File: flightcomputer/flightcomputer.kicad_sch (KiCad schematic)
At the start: 81 parts, among them J1 Conn_Coaxial, J10 Conn_01x03, J11 Conn_01x03, J12 ESQ-113-14-G-D, J13 Conn_01x07, J2 Conn_Coaxial, J3 Conn_Coaxial, J4 Conn_Coaxial, J5 S3B-PH-K-S-GW, J6 S3B-PH-K-S-GW, J7 S4B-PH-K-S_LF__SN_, J8 S3B-PH-K-S-GW, J9 Conn_01x06, U1 MAX-M10S, U2 LIS2MDLTR, U3 BMI088, U4 MS5607-02BA, U5 ESP32-S3-WROOM-1-N4, U7 Teensy4.1, U8 LSM6DSO32TR, U9 RFM96W-433S2

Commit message: resize
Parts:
- removed R16: 0, Resistor_SMD:R_0603_1608Metric_Pad0.98x0.95mm_HandSolder, symbol Device:R
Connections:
- net 5V: no longer J12.13, J12.15, J12.17
- net GND: now also J12.13, J12.15, J12.17; no longer J12.01, J12.03, J12.05
- net PYRO1: no longer J12.24
- net PYRO2: no longer J12.26
- net SENSE_miso: no longer J12.16
- net SENSE_mosi: no longer J12.14
- net SENSE_sck: no longer J12.18
- net aux7_rx: no longer J12.06
- net aux7_tx: no longer J12.08
- net can_rx: no longer J12.10
- net can_tx: no longer J12.12
- net servo1_pwm: no longer J12.22
- net servo2_pwm: no longer J12.20
- net teensy_3.3v: no longer R15.2
- net at J12.04: no longer R15.1
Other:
- moved on the sheet: J12, R15

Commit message: flight computer routing
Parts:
- removed J6, J8: S3B-PH-K-S-GW, HPRlibrary:S3BPHKSGW, symbol HPRlibrary:S3B-PH-K-S-GW
- removed TP15, TP16, TP17, TP18, TP5, TP6, TP7, TP8: TestPoint, Connector_PinHeader_2.54mm:PinHeader_1x01_P2.54mm_Vertical, symbol Connector:TestPoint
- added J14: S3B-PH-K-S-GW, HPRlibrary:S3BPHKSGW, symbol HPRlibrary:S3B-PH-K-S-GW
- added J6, J8: Conn_01x03, Connector_PinHeader_2.54mm:PinHeader_1x03_P2.54mm_Vertical, symbol Connector_Generic:Conn_01x03
- TP1: footprint Connector_PinSocket_2.54mm:PinSocket_1x01_P2.54mm_Vertical -> Connector_PinHeader_2.54mm:PinHeader_1x01_P2.54mm_Vertical
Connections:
- net aux2_rx is gone; now on net PYRO2CONN: U7.9 (7_RX2_OUT1A)
- net aux2_tx is gone; now on net PYRO1CONN: U7.10 (8_TX2_IN1)
- net aux7_rx is gone; now on net lsmimu_int: U7.20 (28_RX7)
- net aux7_tx is gone; now on net lsmimu_cs: U7.21 (29_TX7)
- net 5v_cursns: now also U7.33 (41_A17)
- net 5v_fault: now also U7.32 (40_A16)
- net 6v_cursns: now also U7.45 (23_A9_CRX1_MCLK1)
- net 6v_fault: now also U7.44 (22_A8_CTX1)
- net GND: now also J14.3, J6.1 (Pin_1), J6.2 (Pin_2), J6.3 (Pin_3)
- net PYRO1: now also U7.8 (6_OUT1D); no longer U7.32 (40_A16)
- net PYRO2: now also U7.7 (5_IN2); no longer U7.33 (41_A17)
- net SENSE_miso: now also J8.2 (Pin_2)
- net SENSE_mosi: now also J8.1 (Pin_1)
- net SENSE_sck: now also J8.3 (Pin_3); no longer TP4.1
- net buzz_pwm: now also U7.24 (32_OUT1B); no longer U7.11 (9_OUT1C)
- net can_rx: now also TP4.1, J14.1
- net can_tx: now also TP1.1, J14.2
- net gps_3.3v: no longer R1.1, R2.1
- net imu_accel_int1: now also U7.31 (39_MISO1_OUT1A); no longer U7.16 (24_A10_TX6_SCL2)
- net imu_gyro_int1: now also U7.25 (33_MCLK2); no longer U7.17 (25_A11_RX6_SDA2)
- net lsmimu_cs: no longer U7.44 (22_A8_CTX1)
- net lsmimu_int: no longer U7.45 (23_A9_CRX1_MCLK1)
- net radio_dio1: now also J9.4 (Pin_4); no longer J9.5 (Pin_5)
- net radio_dio2: now also J9.5 (Pin_5); no longer J9.4 (Pin_4)
- net radio_dio3: now also J9.1 (Pin_1); no longer J9.3 (Pin_3)
- net radio_dio5: now also J9.3 (Pin_3); no longer J9.1 (Pin_1)
- net radio_reset: now also U7.11 (9_OUT1C); no longer TP1.1, U7.24 (32_OUT1B)
- net servo1_pwm: now also J12.05
- net servo2_pwm: now also J12.03
- net teensy_3.3v: now also R1.1, R15.1, R2.1
- net x_cursns: now also U7.17 (25_A11_RX6_SDA2)
- net x_fault: now also U7.16 (24_A10_TX6_SCL2)
- net at J12.01: now also R15.2
- no-connect marks 17 -> 13

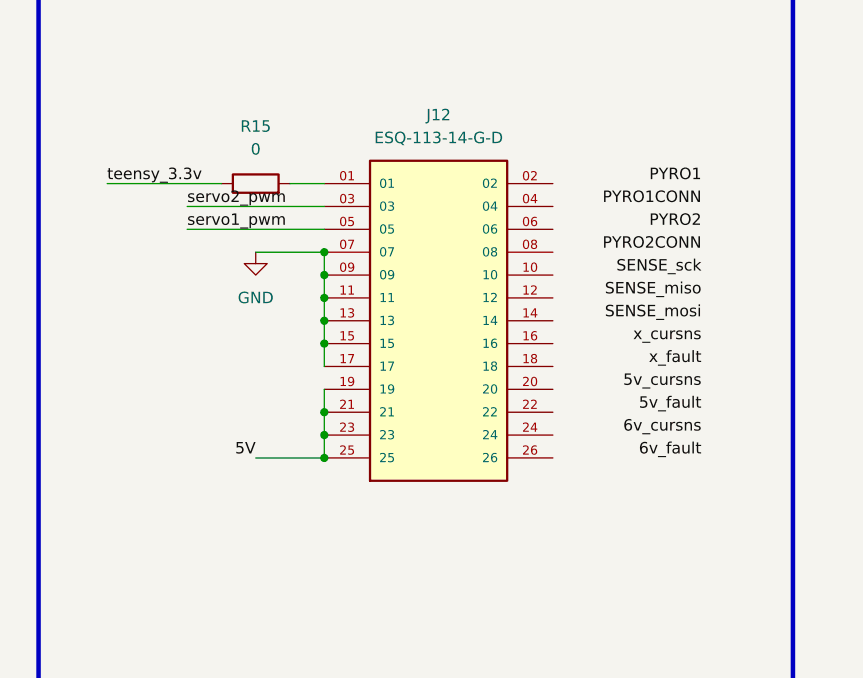
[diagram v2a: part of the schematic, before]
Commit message: hole+connector alignment finish, fc signal routing finish, fc drc warnings related to footprints/silkscreen
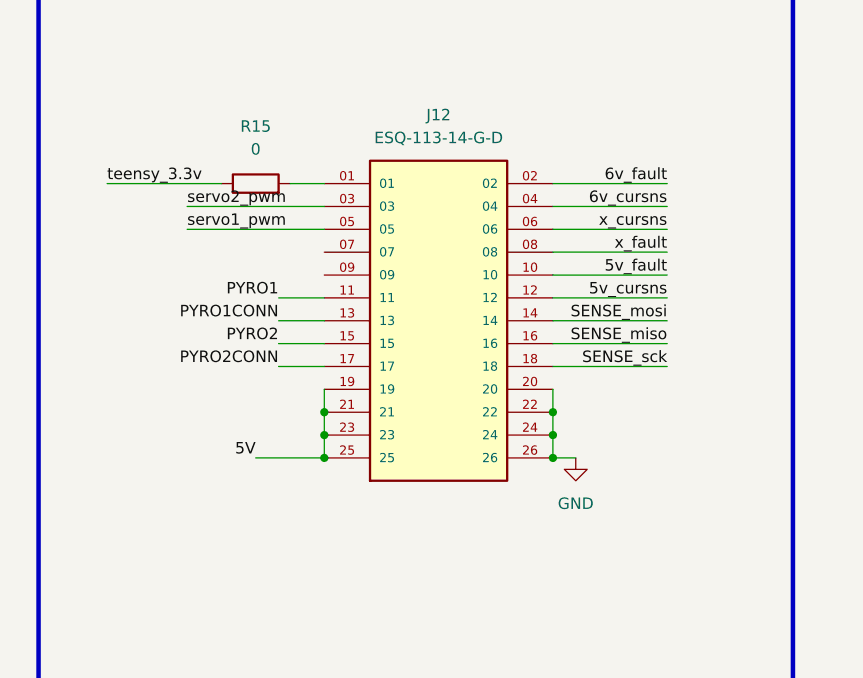
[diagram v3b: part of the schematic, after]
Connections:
- net 5v_cursns: now also J12.12
- net 5v_fault: now also J12.10
- net 6v_cursns: now also J12.04
- net 6v_fault: now also J12.02
- net GND: now also J12.20, J12.22, J12.24, J12.26; no longer J12.07, J12.09, J12.11, J12.13, J12.15, J12.17
- net PYRO1: now also J12.11
- net PYRO1CONN: now also J12.13
- net PYRO2: now also J12.15
- net PYRO2CONN: now also J12.17
- net SENSE_miso: now also J12.16
- net SENSE_mosi: now also J12.14
- net SENSE_sck: now also J12.18
- net x_cursns: now also J12.06
- net x_fault: now also J12.08

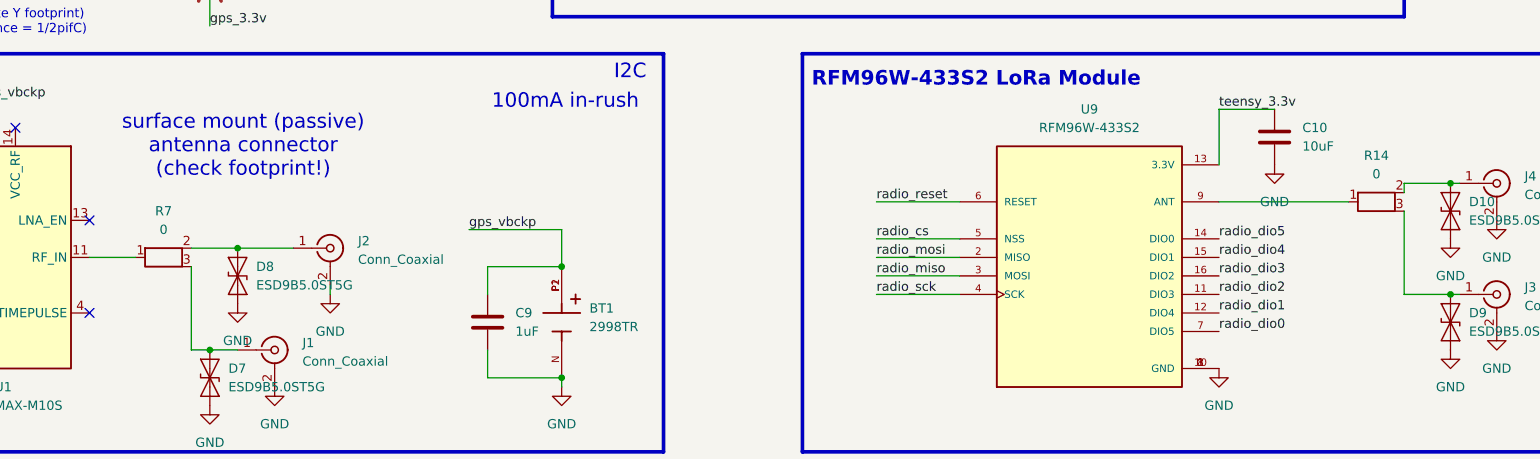
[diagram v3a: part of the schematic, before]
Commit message: killed BMS, updated pyro fets with lower resistance, updated inductor, replace + reroute, fixed some DRC in flight computer (dont know why remaining are being caused, hopefully jlc doesnt care), next todo is to kill myself
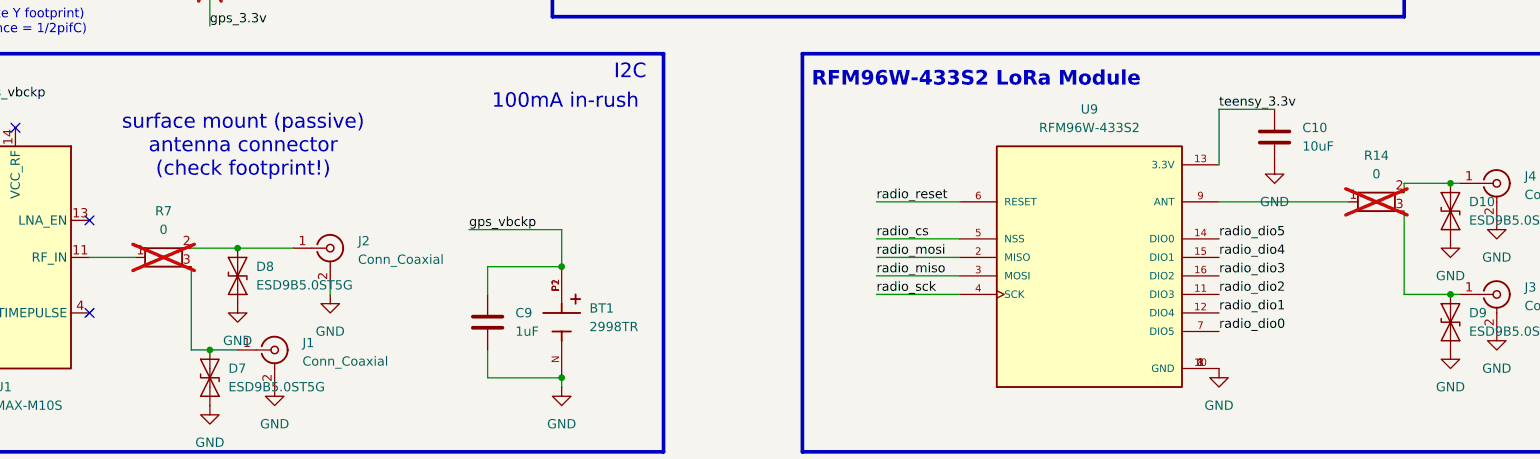
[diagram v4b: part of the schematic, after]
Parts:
- R14, R7: now not fitted
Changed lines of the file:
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@@
 		(in_bom yes)
 		(on_board yes)
-		(dnp no)
+		(dnp yes)
 		(fields_autoplaced yes)
 		(property "Reference" "R7"
@@
 		(in_bom yes)
 		(on_board yes)
-		(dnp no)
+		(dnp yes)
 		(fields_autoplaced yes)
 		(property "Reference" "R14"

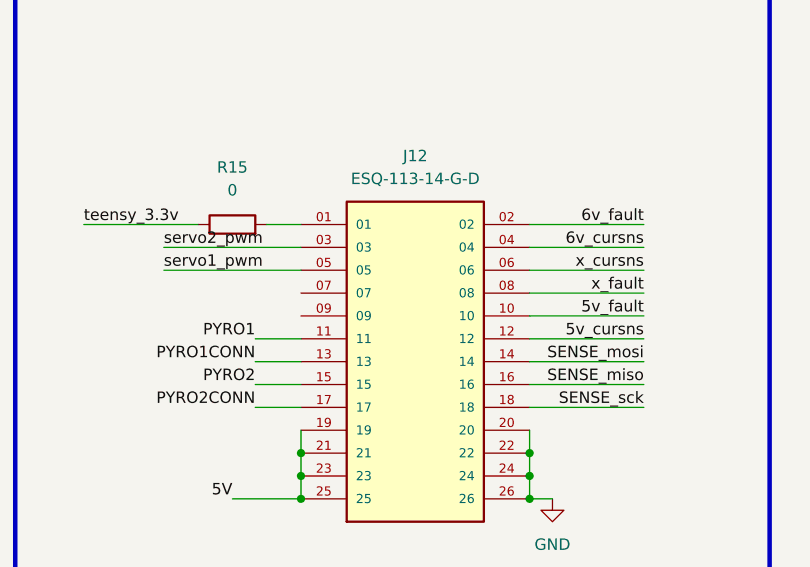
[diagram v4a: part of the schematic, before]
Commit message: changed coax diodes to 0603, reconfigure conn to add 3.3v, added indicator LEDs.
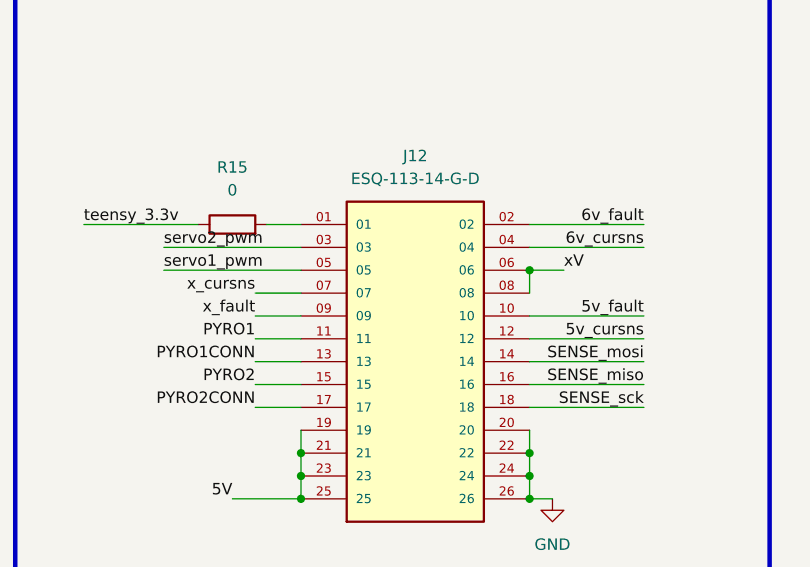
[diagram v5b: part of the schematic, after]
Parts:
- D10, D7, D8, D9: footprint Diode_SMD:D_SOD-923 -> Diode_SMD:D_0603_1608Metric_Pad1.05x0.95mm_HandSolder
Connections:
- net x_cursns: now also J12.07; no longer J12.06
- net x_fault: now also J12.09; no longer J12.08
- new net xV: J12.06, J12.08
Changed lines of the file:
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@@
 	)
 	(junction
+		(at 331.47 142.24)
+		(diameter 0)
+		(color 0 0 0 0)
+	)
+	(junction
 		(at 50.8 124.46)
 		(diameter 0)
@@
 	(wire
 		(pts
+			(xy 300.99 147.32) (xy 306.07 147.32)
+		)
+		(stroke
+			(width 0)
+			(type default)
+		)
+	)
+	(wire
+		(pts
 			(xy 38.1 259.08) (xy 48.26 259.08)
 		)
@@
 	(wire
 		(pts
+			(xy 331.47 142.24) (xy 331.47 144.78)
+		)
+		(stroke
+			(width 0)
+			(type default)
+		)
+	)
+	(wire
+		(pts
 			(xy 306.07 165.1) (xy 306.07 167.64)
 		)
@@
 	(wire
 		(pts
-			(xy 331.47 144.78) (xy 344.17 144.78)
-		)
-		(stroke
-			(width 0)
-			(type default)
-		)
-	)
-	(wire
-		(pts
 			(xy 331.47 152.4) (xy 344.17 152.4)
 		)
@@
 	(wire
 		(pts
+			(xy 331.47 142.24) (xy 335.28 142.24)
+		)
+		(stroke
+			(width 0)
+			(type default)
+		)
+	)
+	(wire
+		(pts
 			(xy 501.65 120.65) (xy 496.57 120.65)
 		)
@@
 	(wire
 		(pts
-			(xy 331.47 142.24) (xy 344.17 142.24)
-		)
-		(stroke
-			(width 0)
-			(type default)
-		)
-	)
-	(wire
-		(pts
 			(xy 226.06 160.02) (xy 240.03 160.02)
 		)
@@
 	(wire
 		(pts
+			(xy 300.99 144.78) (xy 306.07 144.78)
+		)
+		(stroke
+			(width 0)
+			(type default)
+		)
+	)
+	(wire
+		(pts
 			(xy 363.22 240.03) (xy 372.11 240.03)
 		)
@@
 	)
 	(label "x_cursns"
-		(at 344.17 142.24 180)
+		(at 300.99 144.78 180)
 		(effects
 			(font
@@
 		)
 	)
+	(label "xV"
+		(at 335.28 142.24 0)
+		(effects
+			(font
+				(size 1.27 1.27)
+			)
+			(justify left bottom)
+		)
+	)
 	(label "PYRO1"
 		(at 163.83 132.08 180)
@@
 	)
 	(label "x_fault"
-		(at 344.17 144.78 180)
+		(at 300.99 147.32 180)
 		(effects
 			(font
@@
 			)
 		)
-		(property "Footprint" "Diode_SMD:D_SOD-923"
+		(property "Footprint" "Diode_SMD:D_0603_1608Metric_Pad1.05x0.95mm_HandSolder"
 			(at 99.06 256.54 0)
 			(effects
@@
 			)
 		)
-		(property "Footprint" "Diode_SMD:D_SOD-923"
+		(property "Footprint" "Diode_SMD:D_0603_1608Metric_Pad1.05x0.95mm_HandSolder"
 			(at 265.43 247.65 0)
 			(effects
@@
 			)
 		)
-		(property "Footprint" "Diode_SMD:D_SOD-923"
+		(property "Footprint" "Diode_SMD:D_0603_1608Metric_Pad1.05x0.95mm_HandSolder"
 			(at 265.43 262.89 0)
 			(effects
@@
 			)
 		)
-		(property "Footprint" "Diode_SMD:D_SOD-923"
+		(property "Footprint" "Diode_SMD:D_0603_1608Metric_Pad1.05x0.95mm_HandSolder"
 			(at 95.25 270.51 0)
 			(effects

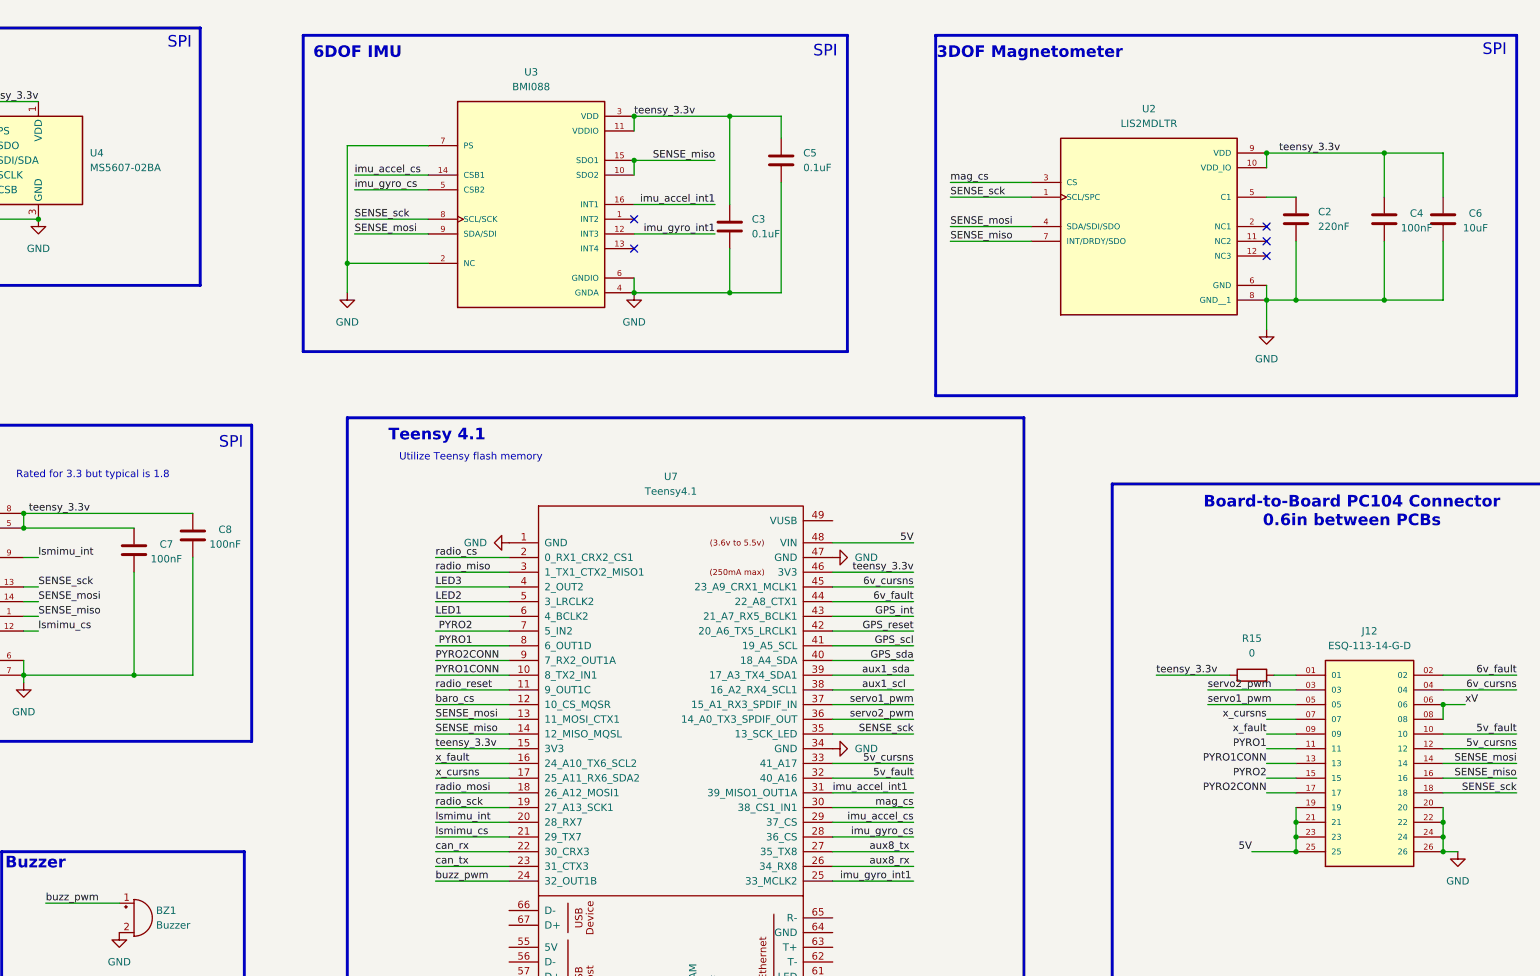
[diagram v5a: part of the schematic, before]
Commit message: schematic notes and placement revisions for order
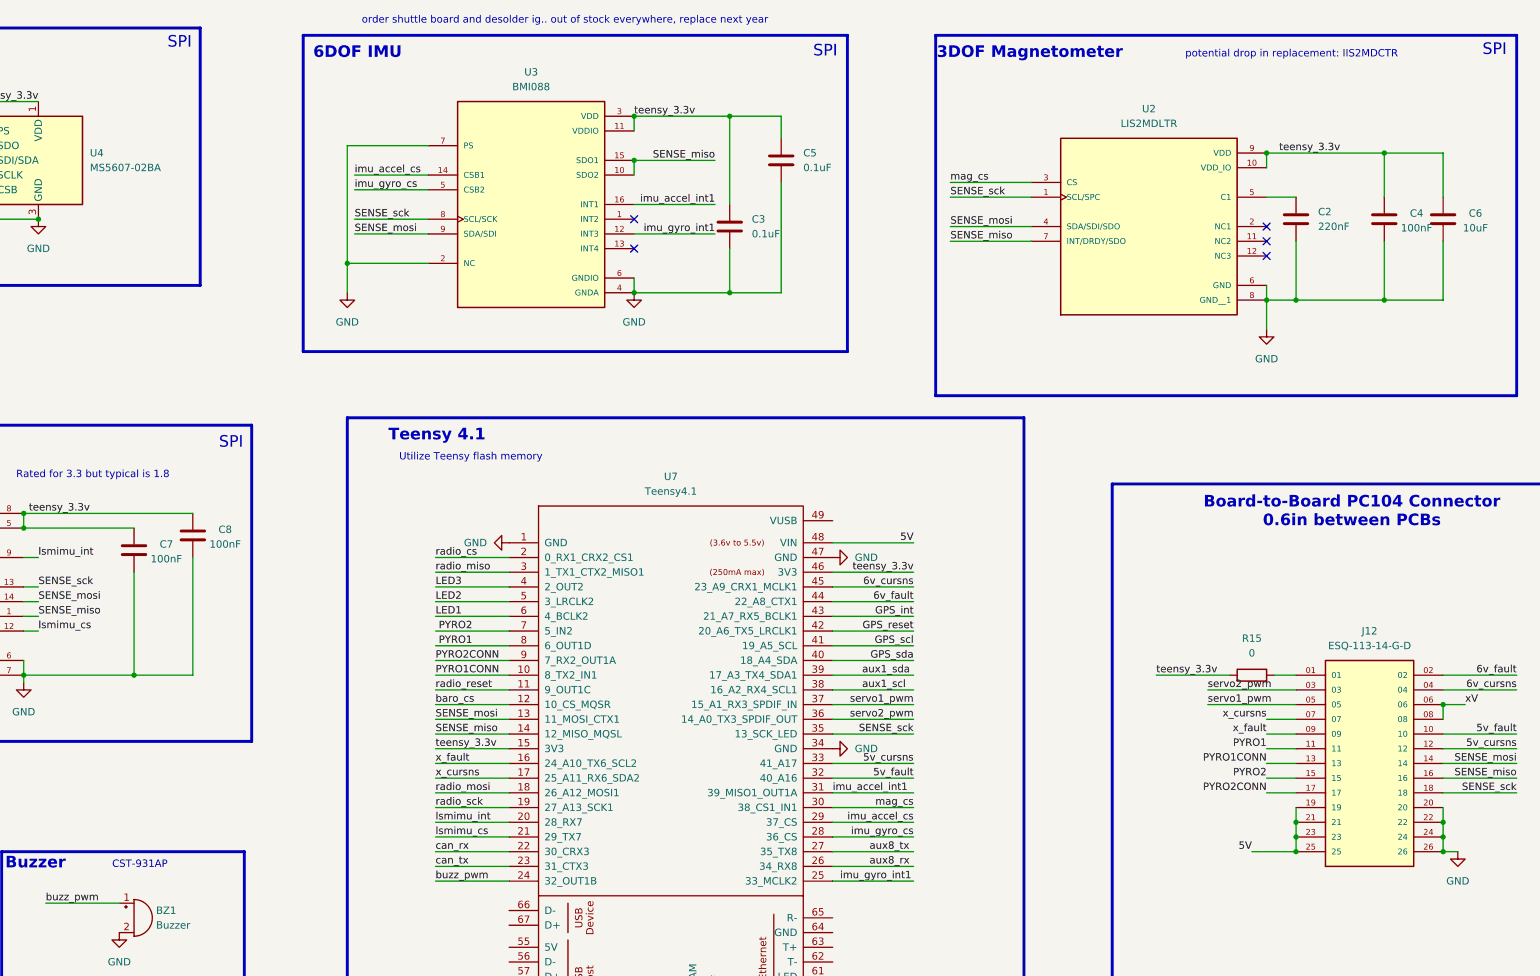
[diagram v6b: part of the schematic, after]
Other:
- note added: "CST-931AP"
- note added: "order shuttle board and desolder ig.. out of stock everywhere, replace next year"
- note added: "potential drop in replacement: IIS2MDCTR"
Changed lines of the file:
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@@
+		)
+	)
+	(text "potential drop in replacement: IIS2MDCTR"
+		(exclude_from_sim no)
+		(at 305.308 29.972 0)
+		(effects
+			(font
+				(size 1.27 1.27)
+			)
 		)
 	)
@@
 		)
 	)
+	(text "CST-931AP"
+		(exclude_from_sim no)
+		(at 106.426 169.926 0)
+		(effects
+			(font
+				(size 1.27 1.27)
+			)
+		)
+	)
 	(text "SPI"
 		(exclude_from_sim no)
@@
 			)
 		)
+	)
+	(text "order shuttle board and desolder ig.. out of stock everywhere, replace next year"
+		(exclude_from_sim no)
+		(at 179.832 24.13 0)
+		(effects
+			(font
+				(size 1.27 1.27)
+			)
+		)
